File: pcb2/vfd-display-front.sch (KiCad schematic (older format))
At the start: 57 parts, among them CON1 AVR-ISP-10, IC1 ATMEGA88A-A, IC2 TD62C950RF, IC3 TD62C950RF, J1 HEADER_5, P1 CONN_02X05, P2 CONN_01X03, P3 CONN_01X02, P4 CONN_01X04, P5 CONN_01X02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

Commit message: Board almost done.
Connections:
- net BTN_WAKE: now also U2.6 (GPIO12)
- net CHG: now also IC1.10 ((PCINT22/OC0A/AIN0)PD6)
- net CK: now also IC1.11 ((PCINT23/AIN1)PD7)
- net CL: now also IC1.14 ((PCINT2/OC1B/~SS~)PB2)
- net S-IN: now also IC1.12 ((PCINT0/CLKO/ICP1)PB0)
- net SPKR: now also IC1.9 ((PCINT21/OC0B/T1)PD5)
- net STB: now also IC1.13 ((PCINT1/OC1A)PB1)
- no-connect marks 11 -> 29
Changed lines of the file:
@@
 Entry Wire Line
 	9950 5050 10050 5150
-Entry Wire Line
-	9950 5150 10050 5250
-Entry Wire Line
-	9950 5250 10050 5350
 Text Label 9800 3250 0    60   ~ 0
 G21
@@
 Text Label 4500 1300 1    60   ~ 0
 SCK
-Entry Wire Line
-	4300 2900 4400 2800
-Text Label 4100 2900 0    60   ~ 0
+Text Label 5850 2900 0    60   ~ 0
 RST
 $Comp
@@
 L GND #PWR023
 U 1 1 57807930
-P 5150 2500
-F 0 "#PWR023" H 5150 2250 50  0001 C CNN
-F 1 "GND" H 5150 2350 50  0000 C CNN
-F 2 "" H 5150 2500 50  0000 C CNN
-F 3 "" H 5150 2500 50  0000 C CNN
-	1    5150 2500
+P 5150 2450
+F 0 "#PWR023" H 5150 2200 50  0001 C CNN
+F 1 "GND" H 5150 2300 50  0000 C CNN
+F 2 "" H 5150 2450 50  0000 C CNN
+F 3 "" H 5150 2450 50  0000 C CNN
+	1    5150 2450
 	1    0    0    -1
 $EndComp
@@
 L GND #PWR024
 U 1 1 57807992
-P 5650 2500
-F 0 "#PWR024" H 5650 2250 50  0001 C CNN
-F 1 "GND" H 5650 2350 50  0000 C CNN
-F 2 "" H 5650 2500 50  0000 C CNN
-F 3 "" H 5650 2500 50  0000 C CNN
-	1    5650 2500
+P 5650 2450
+F 0 "#PWR024" H 5650 2200 50  0001 C CNN
+F 1 "GND" H 5650 2300 50  0000 C CNN
+F 2 "" H 5650 2450 50  0000 C CNN
+F 3 "" H 5650 2450 50  0000 C CNN
+	1    5650 2450
 	1    0    0    -1
 $EndComp
@@
 	9500 5050 9950 5050
 Wire Wire Line
-	9950 5150 9500 5150
-Wire Wire Line
-	9500 5250 9950 5250
-Wire Wire Line
 	9950 1550 9500 1550
 Wire Wire Line
@@
 	4300 1750 3550 1750
 Wire Wire Line
-	4300 2900 3550 2900
+	3550 2900 6050 2900
 Wire Bus Line
 	4100 7800 4100 10250
@@
 	3550 2150 5650 2150
 Wire Wire Line
-	5650 2450 5650 2500
-Wire Wire Line
-	5150 2500 5150 2450
+	5650 2450 5650 2450
+Wire Wire Line
+	5150 2450 5150 2450
 Wire Wire Line
 	8950 8850 8950 8800
@@
 	4500 1950 4500 1050
 Wire Wire Line
-	3550 2700 4100 2700
-Wire Wire Line
-	3550 2800 4100 2800
-Text Label 3900 2700 0    60   ~ 0
+	3550 2700 6050 2700
+Wire Wire Line
+	3550 2800 6050 2800
+Text Label 5850 2700 0    60   ~ 0
 SDA
-Text Label 3900 2800 0    60   ~ 0
+Text Label 5850 2800 0    60   ~ 0
 SCL
 NoConn ~ 1650 2050
@@
 BTN_ENC
 NoConn ~ 11300 2350
+Entry Wire Line
+	4100 950  4200 1050
+Wire Wire Line
+	3550 1650 4200 1650
+Wire Wire Line
+	4200 1650 4200 1050
+Text Label 4200 1300 1    60   ~ 0
+CL
+Entry Wire Line
+	4000 950  4100 1050
+Entry Wire Line
+	3900 950  4000 1050
+Wire Wire Line
+	3550 1550 4100 1550
+Wire Wire Line
+	4100 1550 4100 1050
+Wire Wire Line
+	3550 1450 4000 1450
+Wire Wire Line
+	4000 1450 4000 1050
+Text Label 4100 1300 1    60   ~ 0
+STB
+Text Label 4000 1300 1    60   ~ 0
+S-IN
+Entry Wire Line
+	6050 3750 6150 3850
+Wire Wire Line
+	6050 3750 3550 3750
+Text Label 5800 3750 0    60   ~ 0
+CK
+Entry Wire Line
+	6050 3650 6150 3750
+Wire Wire Line
+	6050 3650 3550 3650
+Text Label 5800 3650 0    60   ~ 0
+CHG
+Entry Wire Line
+	6050 2700 6150 2800
+Entry Wire Line
+	6050 2800 6150 2900
+Entry Wire Line
+	6050 2900 6150 3000
+Entry Wire Line
+	6050 3550 6150 3650
+Wire Wire Line
+	6050 3550 3550 3550
+Text Label 5800 3550 0    60   ~ 0
+SPKR
+Entry Wire Line
+	6050 7000 6150 7100
+Wire Wire Line
+	6050 7000 1400 7000
+Wire Wire Line
+	1400 7000 1400 5900
+Wire Wire Line
+	1400 5900 1850 5900
+Text Label 5600 7000 0    60   ~ 0
+BTN_WAKE
+NoConn ~ 9500 5150
+NoConn ~ 9500 5250
+NoConn ~ 12500 1550
+NoConn ~ 12500 1650
+NoConn ~ 3550 3450
+NoConn ~ 3550 3050
+NoConn ~ 3550 2300
+NoConn ~ 3550 2400
+NoConn ~ 3550 2500
+NoConn ~ 3550 2600
+NoConn ~ 3650 5900
+NoConn ~ 1850 6000
+NoConn ~ 2500 6600
+NoConn ~ 2600 6600
+NoConn ~ 2700 6600
+NoConn ~ 2800 6600
+NoConn ~ 2900 6600
+NoConn ~ 3000 6600
 $EndSCHEMATC

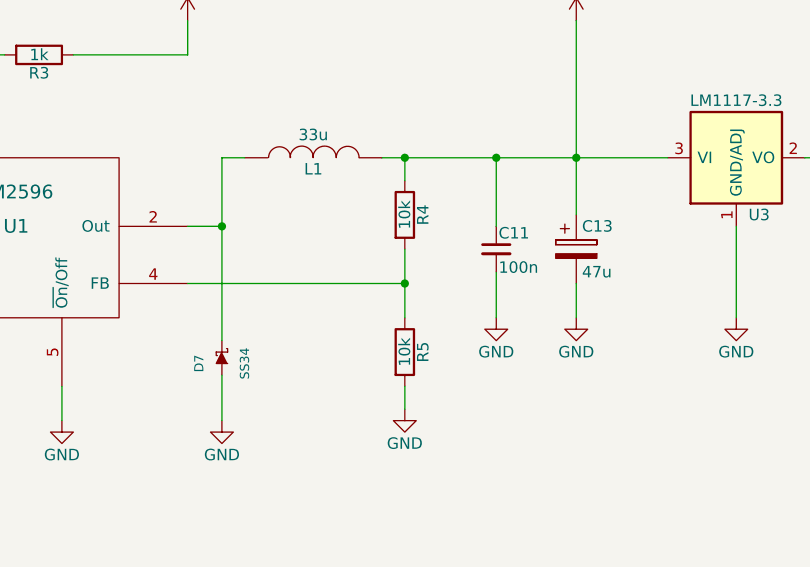
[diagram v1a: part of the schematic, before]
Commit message: Update resistor values.
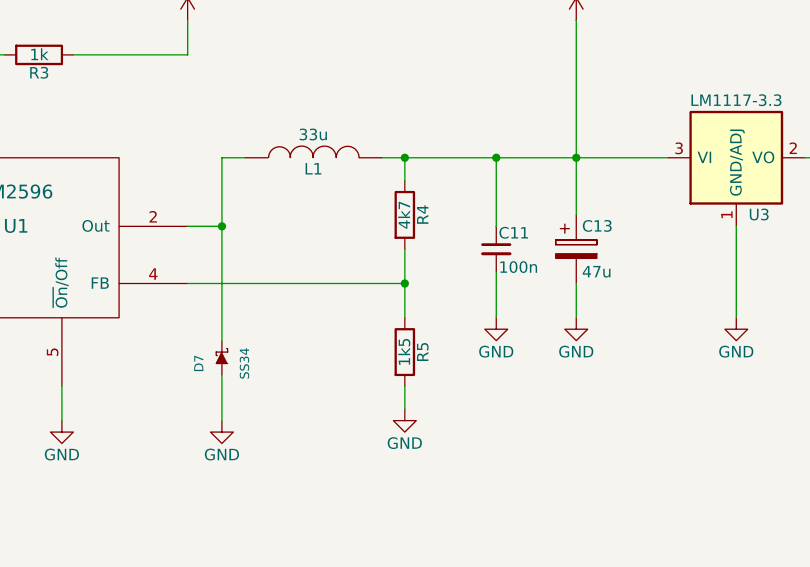
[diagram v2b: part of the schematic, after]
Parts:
- R4: value 10k -> 4k7
- R5: value 10k -> 1k5
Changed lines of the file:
@@
 P 12950 8350
 F 0 "R4" V 13030 8350 50  0000 C CNN
-F 1 "10k" V 12950 8350 50  0000 C CNN
+F 1 "4k7" V 12950 8350 50  0000 C CNN
 F 2 "Resistors_SMD:R_1206_HandSoldering" V 12880 8350 50  0001 C CNN
 F 3 "" H 12950 8350 50  0000 C CNN
@@
 P 12950 8950
 F 0 "R5" V 13030 8950 50  0000 C CNN
-F 1 "10k" V 12950 8950 50  0000 C CNN
+F 1 "1k5" V 12950 8950 50  0000 C CNN
 F 2 "Resistors_SMD:R_1206_HandSoldering" V 12880 8950 50  0001 C CNN
 F 3 "" H 12950 8950 50  0000 C CNN

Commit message: Add correct footprint for PCB. Fix PCB.
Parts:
- IC2, IC3: footprint futaba-vfd:futaba-vfd-SSOP60-P-0.65 -> TD62C950RF:SSOP60-P-0.65A
